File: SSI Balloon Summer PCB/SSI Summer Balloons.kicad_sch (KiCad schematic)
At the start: 0 parts

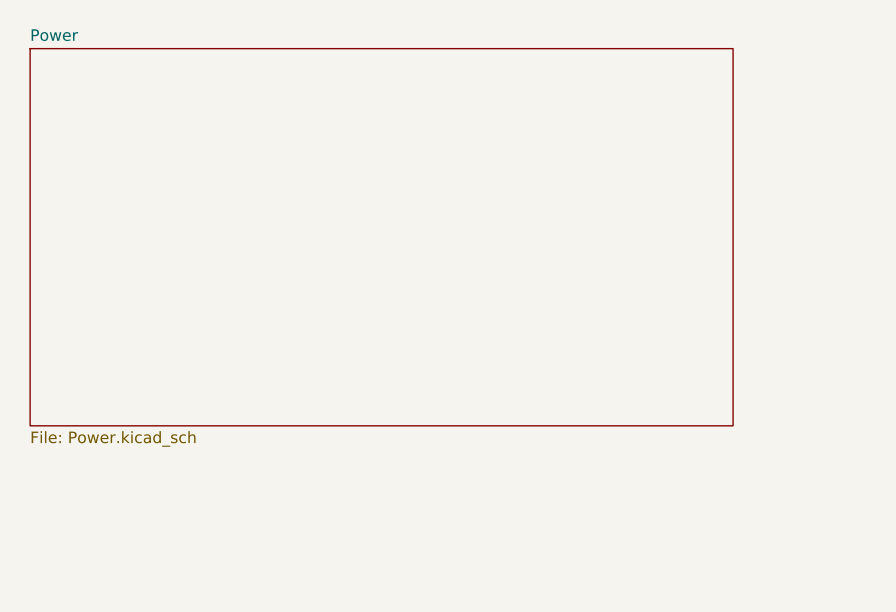
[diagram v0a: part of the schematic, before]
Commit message: Worked on LoRa and APRS
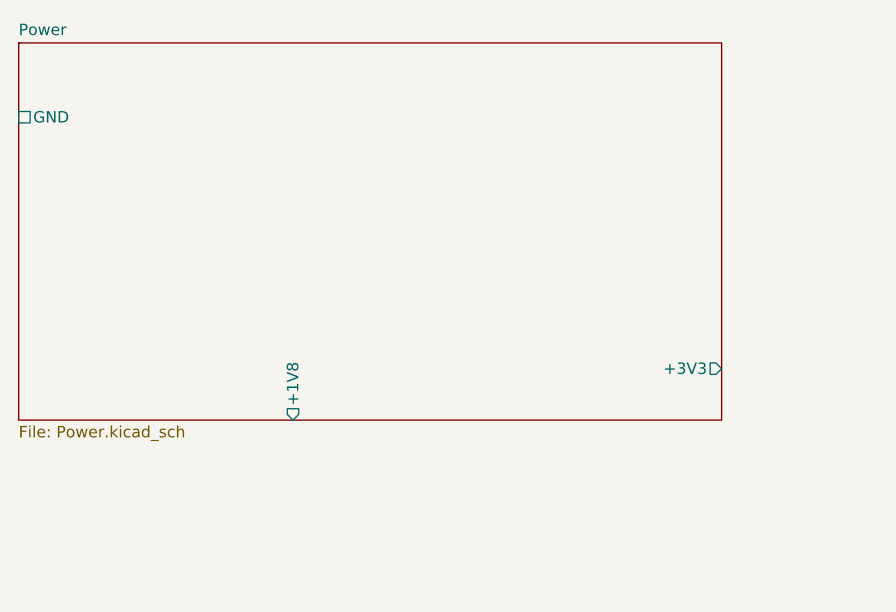
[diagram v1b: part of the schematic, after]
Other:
- sheet Power ports: added +1V8, +3V3, GND; removed none
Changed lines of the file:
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@@
 		)
 		(instances
-			(project "Untitled"
+			(project "SSI Summer Balloons"
 				(path "/3c45a535-6e6b-4825-ad52-82c10cbe7866"
 					(page "4")
@@
 	)
 	(sheet
-		(at 21.59 34.925)
+		(at 20.32 34.29)
 		(size 78.105 41.91)
 		(exclude_from_sim no)
@@
 		)
 		(property "Sheetname" "Power"
-			(at 21.59 34.2134 0)
+			(at 20.32 33.5784 0)
 			(show_name no)
 			(do_not_autoplace no)
@@
 		)
 		(property "Sheetfile" "Power.kicad_sch"
-			(at 21.59 77.4196 0)
-			(show_name no)
-			(do_not_autoplace no)
-			(effects
-				(font
-					(size 1.27 1.27)
-				)
-				(justify left top)
-			)
-		)
-		(instances
-			(project "Untitled"
+			(at 20.32 76.7846 0)
+			(show_name no)
+			(do_not_autoplace no)
+			(effects
+				(font
+					(size 1.27 1.27)
+				)
+				(justify left top)
+			)
+		)
+		(pin "+1V8" output
+			(at 50.8 76.2 270)
+			(effects
+				(font
+					(size 1.27 1.27)
+				)
+				(justify left)
+			)
+		)
+		(pin "+3V3" output
+			(at 98.425 70.485 0)
+			(effects
+				(font
+					(size 1.27 1.27)
+				)
+				(justify right)
+			)
+		)
+		(pin "GND" passive
+			(at 20.32 42.545 180)
+			(effects
+				(font
+					(size 1.27 1.27)
+				)
+				(justify left)
+			)
+		)
+		(instances
+			(project "SSI Summer Balloons"
 				(path "/3c45a535-6e6b-4825-ad52-82c10cbe7866"
 					(page "2")
@@
 		)
 		(instances
-			(project "Untitled"
+			(project "SSI Summer Balloons"
 				(path "/3c45a535-6e6b-4825-ad52-82c10cbe7866"
 					(page "5")
@@
 		)
 		(instances
-			(project "Untitled"
+			(project "SSI Summer Balloons"
 				(path "/3c45a535-6e6b-4825-ad52-82c10cbe7866"
 					(page "6")
@@
 		)
 		(instances
-			(project "Untitled"
+			(project "SSI Summer Balloons"
 				(path "/3c45a535-6e6b-4825-ad52-82c10cbe7866"
 					(page "3")

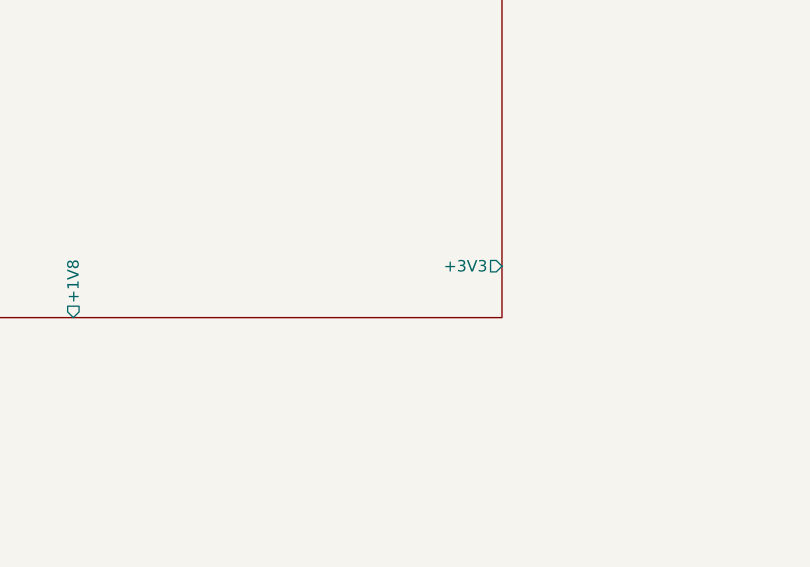
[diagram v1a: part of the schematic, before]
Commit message: Added 4.1V rail for APRS
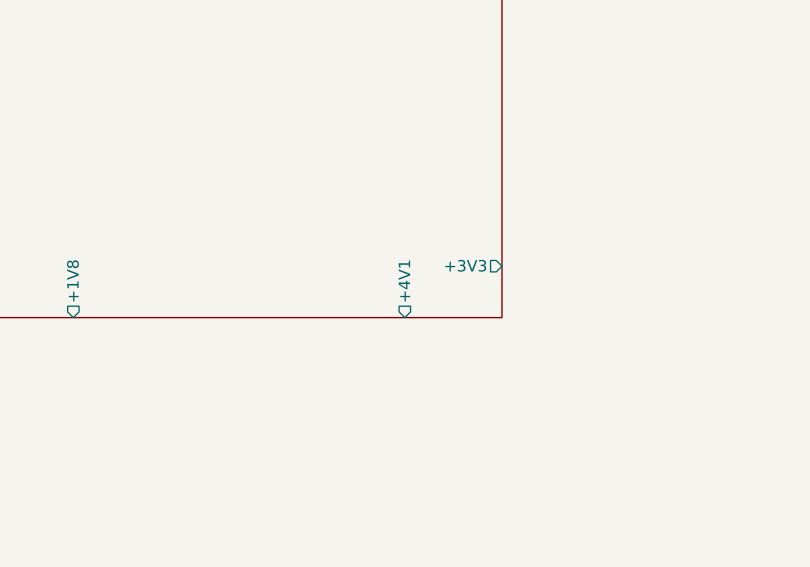
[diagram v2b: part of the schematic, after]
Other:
- sheet Power ports: added +4V1; removed none
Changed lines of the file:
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@@
+			)
+		)
+		(pin "+4V1" output
+			(at 87.63 76.2 270)
+			(effects
+				(font
+					(size 1.27 1.27)
+				)
+				(justify left)
 			)
 		)

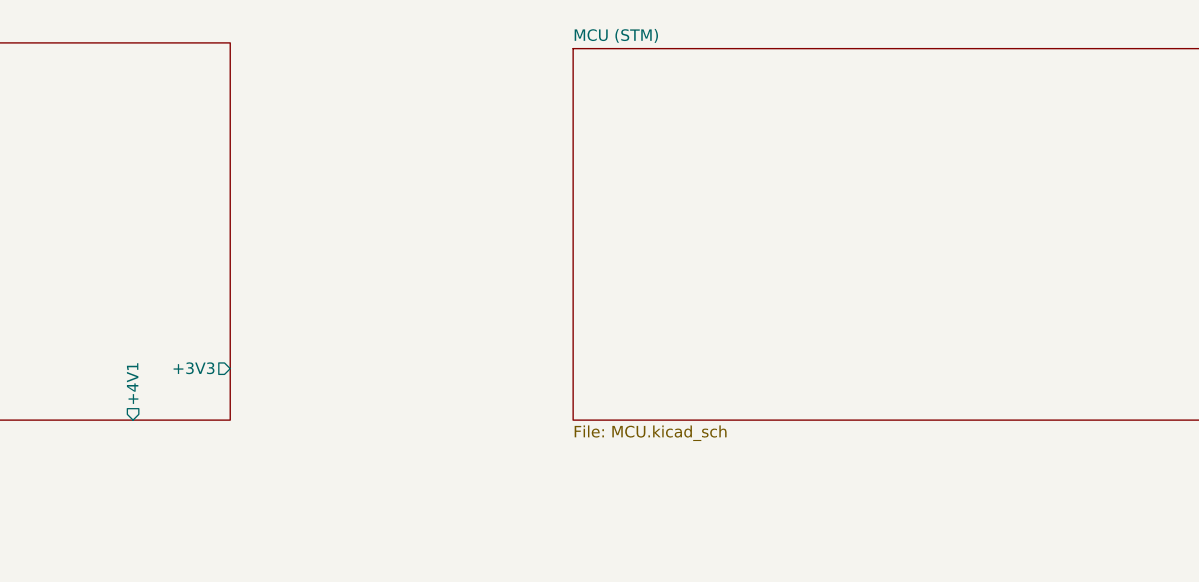
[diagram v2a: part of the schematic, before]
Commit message: Added CS pins for SPI and hierarchical labels to MCU sheet
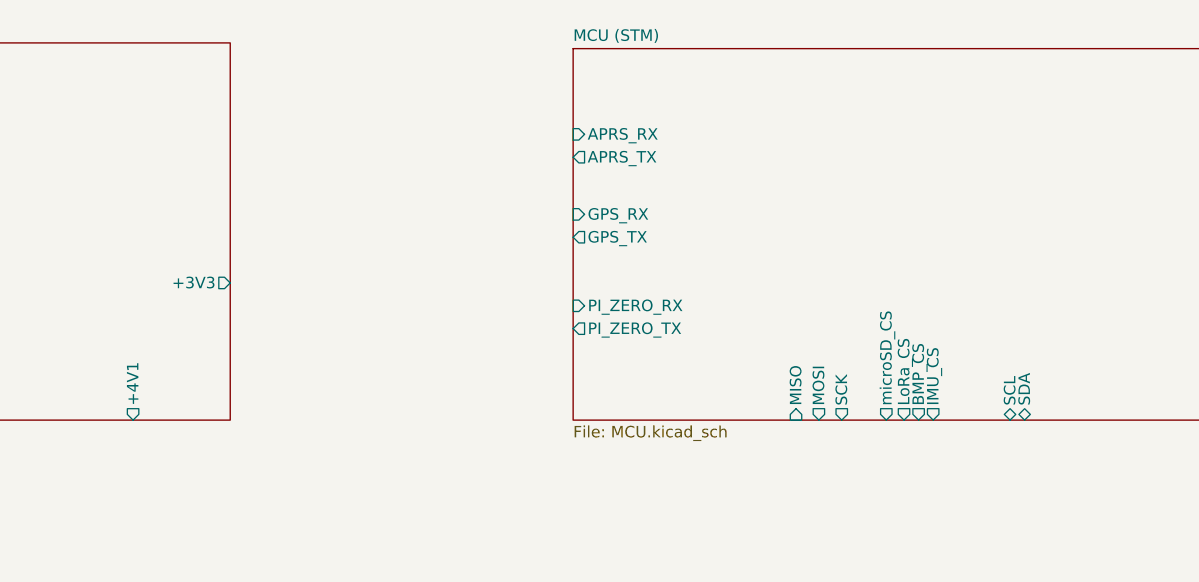
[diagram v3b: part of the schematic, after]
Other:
- sheet MCU (STM) ports: added APRS_RX, APRS_TX, BMP_CS, GPS_RX, GPS_TX, IMU_CS, LoRa_CS, MISO, MOSI, PI_ZERO_RX, PI_ZERO_TX, SCK, SCL, SDA, microSD_CS; removed none
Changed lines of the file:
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@@
 		)
 		(pin "+3V3" output
-			(at 98.425 70.485 0)
+			(at 98.425 60.96 0)
 			(effects
 				(font
@@
 			)
 		)
+		(pin "GPS_RX" input
+			(at 136.525 53.34 180)
+			(effects
+				(font
+					(size 1.27 1.27)
+				)
+				(justify left)
+			)
+		)
+		(pin "MISO" input
+			(at 161.29 76.2 270)
+			(effects
+				(font
+					(size 1.27 1.27)
+				)
+				(justify left)
+			)
+		)
+		(pin "MOSI" output
+			(at 163.83 76.2 270)
+			(effects
+				(font
+					(size 1.27 1.27)
+				)
+				(justify left)
+			)
+		)
+		(pin "APRS_RX" input
+			(at 136.525 44.45 180)
+			(effects
+				(font
+					(size 1.27 1.27)
+				)
+				(justify left)
+			)
+		)
+		(pin "PI_ZERO_RX" input
+			(at 136.525 63.5 180)
+			(effects
+				(font
+					(size 1.27 1.27)
+				)
+				(justify left)
+			)
+		)
+		(pin "microSD_CS" output
+			(at 171.3228 76.2 270)
+			(effects
+				(font
+					(size 1.27 1.27)
+				)
+				(justify left)
+			)
+		)
+		(pin "PI_ZERO_TX" output
+			(at 136.525 66.04 180)
+			(effects
+				(font
+					(size 1.27 1.27)
+				)
+				(justify left)
+			)
+		)
+		(pin "LoRa_CS" output
+			(at 173.2914 76.2 270)
+			(effects
+				(font
+					(size 1.27 1.27)
+				)
+				(justify left)
+			)
+		)
+		(pin "BMP_CS" output
+			(at 174.9107 76.2 270)
+			(effects
+				(font
+					(size 1.27 1.27)
+				)
+				(justify left)
+			)
+		)
+		(pin "IMU_CS" output
+			(at 176.53 76.2 270)
+			(effects
+				(font
+					(size 1.27 1.27)
+				)
+				(justify left)
+			)
+		)
+		(pin "SCK" output
+			(at 166.37 76.2 270)
+			(effects
+				(font
+					(size 1.27 1.27)
+				)
+				(justify left)
+			)
+		)
+		(pin "GPS_TX" output
+			(at 136.525 55.88 180)
+			(effects
+				(font
+					(size 1.27 1.27)
+				)
+				(justify left)
+			)
+		)
+		(pin "APRS_TX" output
+			(at 136.525 46.99 180)
+			(effects
+				(font
+					(size 1.27 1.27)
+				)
+				(justify left)
+			)
+		)
+		(pin "SCL" bidirectional
+			(at 185.0707 76.2 270)
+			(effects
+				(font
+					(size 1.27 1.27)
+				)
+				(justify left)
+			)
+		)
+		(pin "SDA" bidirectional
+			(at 186.69 76.2 270)
+			(effects
+				(font
+					(size 1.27 1.27)
+				)
+				(justify left)
+			)
+		)

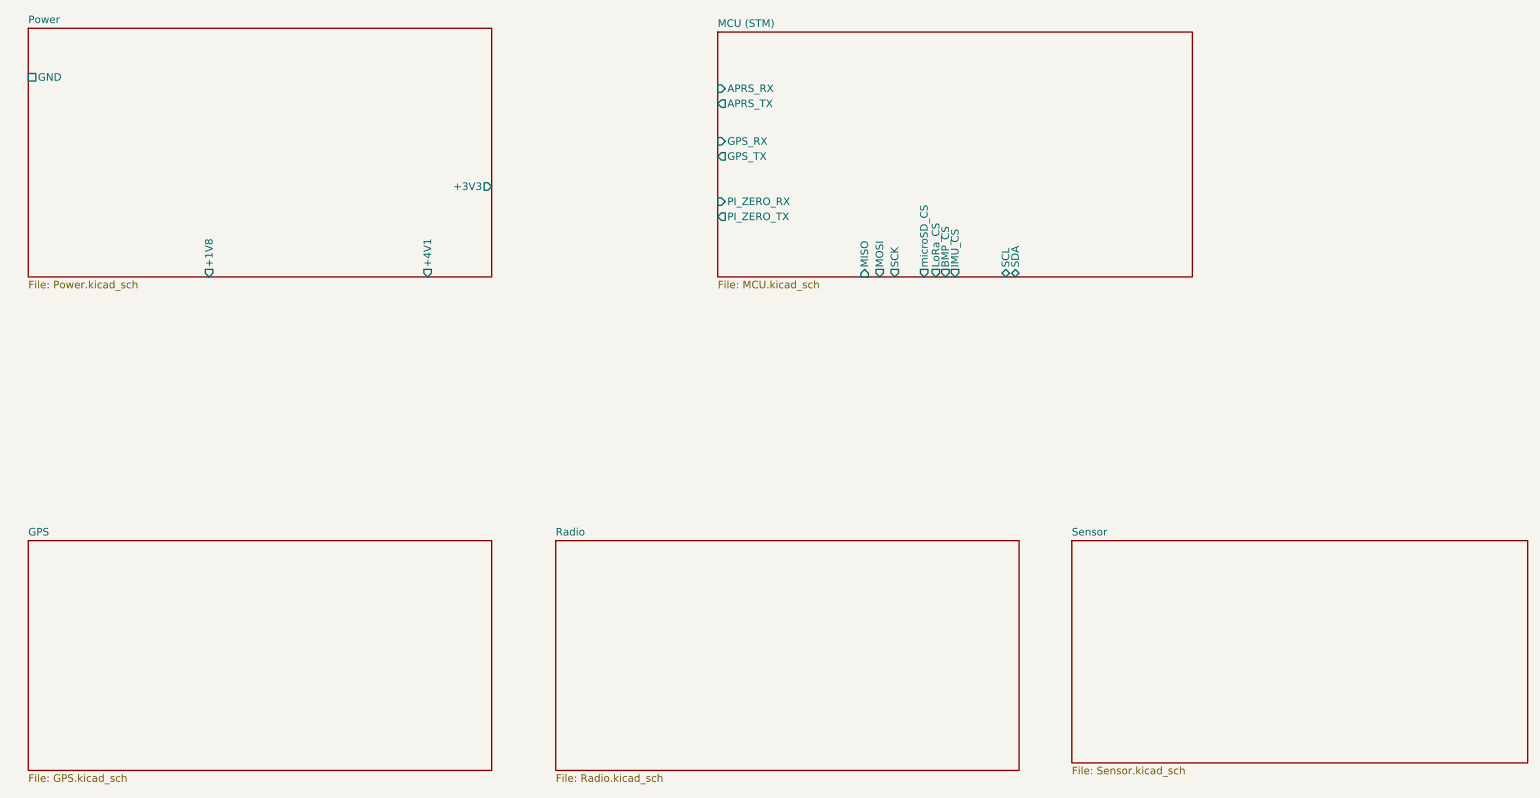
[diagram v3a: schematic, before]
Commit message: Standardized power symbols, added microSD sheet, and standardized hierarchical labels
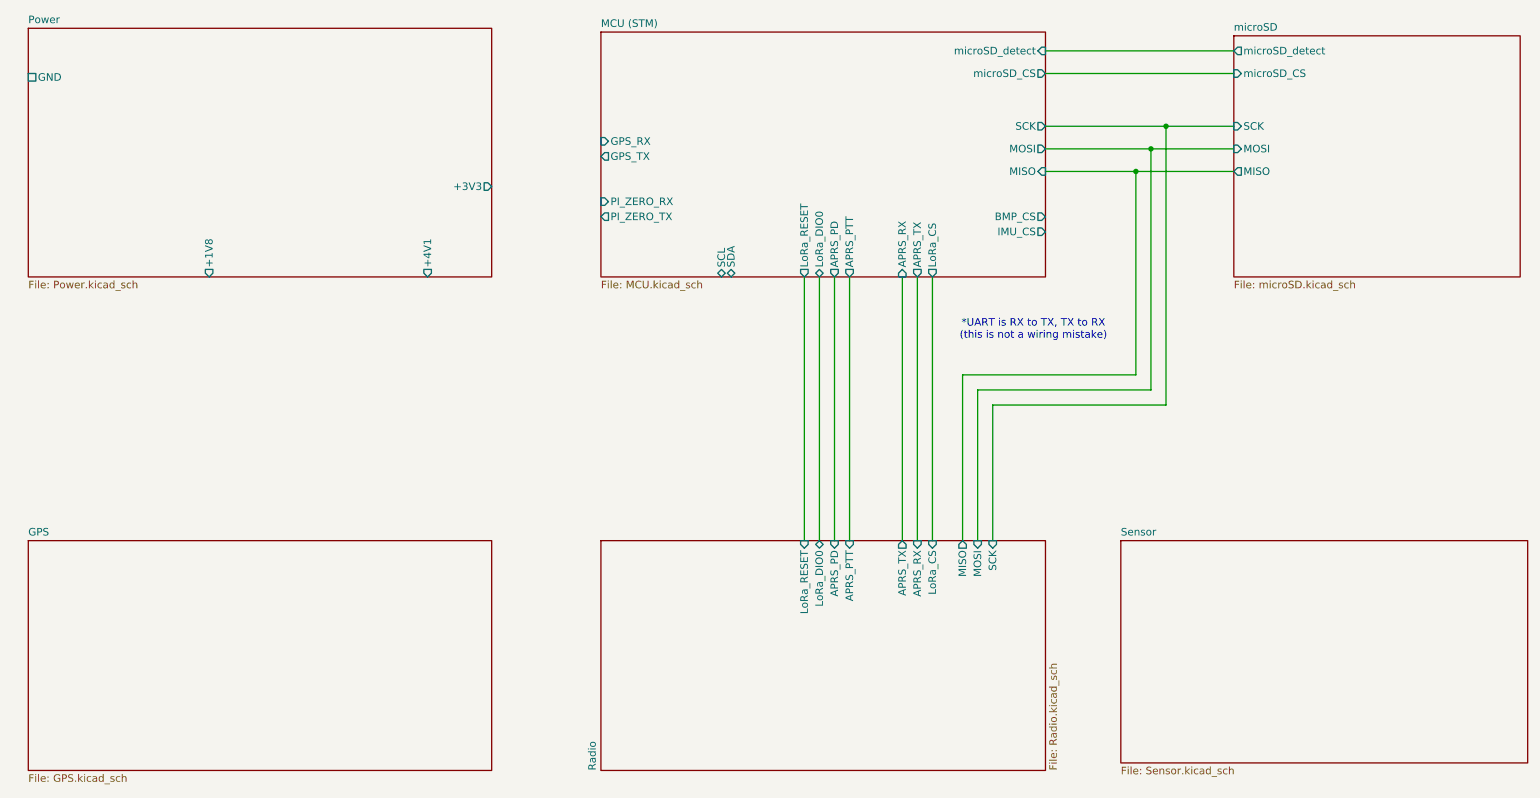
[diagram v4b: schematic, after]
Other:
- added sheet microSD (microSD.kicad_sch)
- sheet MCU (STM) ports: added APRS_PD, APRS_PTT, LoRa_DIO0, LoRa_RESET, microSD_detect; removed none
- sheet Radio ports: added APRS_PD, APRS_PTT, APRS_RX, APRS_TX, LoRa_CS, LoRa_DIO0, LoRa_RESET, MISO, MOSI, SCK; removed none
- note added: "*UART is RX to TX, TX to RX (this is not a wiring mistake)"

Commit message: schematic
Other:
- sheet MCU (STM) ports: added +3V3; removed none
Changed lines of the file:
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@@
+	)
+	(junction
+		(at 98.425 69.85)
+		(diameter 0)
+		(color 0 0 0 0)
 	)
 	(junction
@@
 	(wire
 		(pts
+			(xy 97.79 69.85) (xy 98.425 69.85)
+		)
+		(stroke
+			(width 0)
+			(type default)
+		)
+	)
+	(wire
+		(pts
 			(xy 170.18 76.2) (xy 170.18 120.65)
 		)
@@
 		(pts
 			(xy 172.72 76.2) (xy 172.72 120.65)
+		)
+		(stroke
+			(width 0)
+			(type default)
+		)
+	)
+	(wire
+		(pts
+			(xy 98.425 69.85) (xy 116.84 69.85)
 		)
 		(stroke
@@
 		)
 		(pin "+3V3" output
-			(at 98.425 60.96 0)
+			(at 98.425 69.85 0)
 			(effects
 				(font
@@
 			(effects
 				(font
+					(size 1.27 1.27)
+				)
+				(justify left)
+			)
+		)
+		(pin "+3V3" input
+			(at 116.84 69.85 180)
+			(effects
+				(font
